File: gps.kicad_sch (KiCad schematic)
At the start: 7 parts

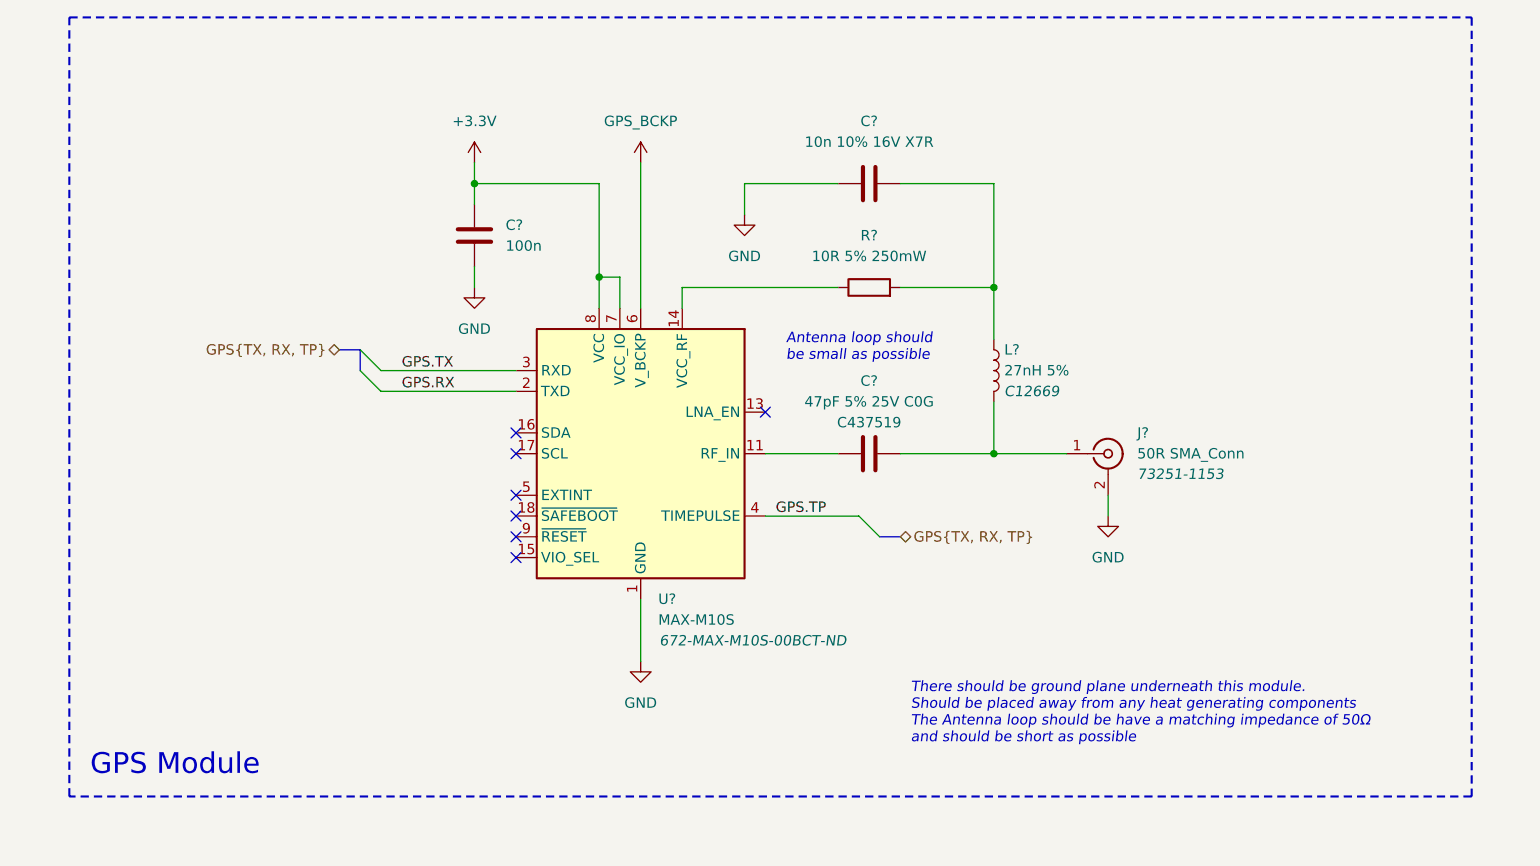
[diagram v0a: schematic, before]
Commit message: display driver update
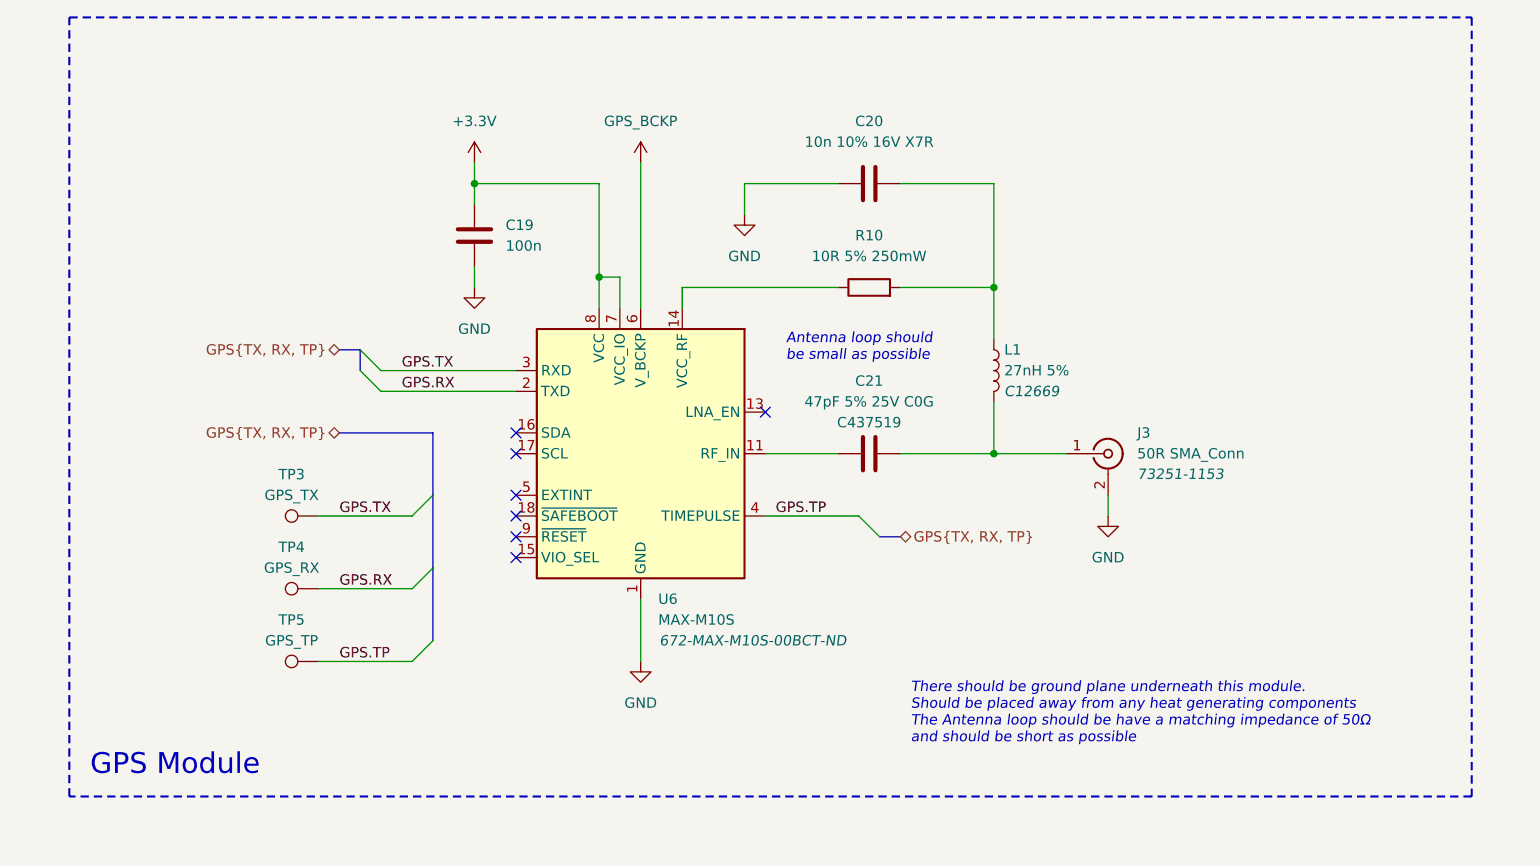
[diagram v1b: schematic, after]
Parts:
- added TP3: GPS_TX, TestPoint:TestPoint_Pad_D1.0mm, symbol Connector:TestPoint
- added TP4: GPS_RX, TestPoint:TestPoint_Pad_D1.0mm, symbol Connector:TestPoint
- added TP5: GPS_TP, TestPoint:TestPoint_Pad_D1.0mm, symbol Connector:TestPoint
- gave numbers to parts that had none: 7
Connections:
- net GPS.RX: now also TP4.1
- net GPS.TP: now also TP5.1
- net GPS.TX: now also TP3.1

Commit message: Display Driver Completion
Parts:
- C19: renamed from C21; footprint (none) -> Capacitor_SMD:C_0402_1005Metric
- renumbered C19 to C17, C20 to C18, R10 to R3, TP3 to TP1, TP4 to TP2, TP5 to TP3, U6 to U4
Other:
- moved on the sheet: TP1, TP2, TP3

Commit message: PCB Routing
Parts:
- renumbered C17 to C19, C18 to C20, C19 to C21, U4 to U5
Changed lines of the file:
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@@
 		(dnp no)
 		(fields_autoplaced yes)
-		(property "Reference" "C18"
+		(property "Reference" "C20"
 			(at 167.64 63.5 90)
 			(effects
@@
 			(project "Precision Clock"
 				(path "/c9a8ff63-a0d1-4125-9dd1-40fb53daf536/adbcdd61-c016-4293-925d-555ee31f0e50"
-					(reference "C18")
+					(reference "C20")
 					(unit 1)
 				)
@@
 		(dnp no)
 		(fields_autoplaced yes)
-		(property "Reference" "#PWR043"
+		(property "Reference" "#PWR046"
 			(at 119.38 72.39 0)
 			(effects
@@
 			(project "Precision Clock"
 				(path "/c9a8ff63-a0d1-4125-9dd1-40fb53daf536/adbcdd61-c016-4293-925d-555ee31f0e50"
-					(reference "#PWR043")
+					(reference "#PWR046")
 					(unit 1)
 				)
@@
 		(dnp no)
 		(fields_autoplaced yes)
-		(property "Reference" "#PWR048"
+		(property "Reference" "#PWR051"
 			(at 196.85 118.11 0)
 			(effects
@@
 			(project "Precision Clock"
 				(path "/c9a8ff63-a0d1-4125-9dd1-40fb53daf536/adbcdd61-c016-4293-925d-555ee31f0e50"
-					(reference "#PWR048")
+					(reference "#PWR051")
 					(unit 1)
 				)
@@
 		(on_board yes)
 		(dnp no)
-		(property "Reference" "C19"
+		(property "Reference" "C21"
 			(at 167.64 95.25 90)
 			(effects
@@
 			(project ""
 				(path "/c9a8ff63-a0d1-4125-9dd1-40fb53daf536/adbcdd61-c016-4293-925d-555ee31f0e50"
-					(reference "C19")
+					(reference "C21")
 					(unit 1)
 				)
@@
 		(dnp no)
 		(fields_autoplaced yes)
-		(property "Reference" "C17"
+		(property "Reference" "C19"
 			(at 123.19 76.1999 0)
 			(effects
@@
 			(project "Precision Clock"
 				(path "/c9a8ff63-a0d1-4125-9dd1-40fb53daf536/adbcdd61-c016-4293-925d-555ee31f0e50"
-					(reference "C17")
+					(reference "C19")
 					(unit 1)
 				)
@@
 		(dnp no)
 		(fields_autoplaced yes)
-		(property "Reference" "#PWR046"
+		(property "Reference" "#PWR049"
 			(at 139.7 135.89 0)
 			(effects
@@
 			(project "Precision Clock"
 				(path "/c9a8ff63-a0d1-4125-9dd1-40fb53daf536/adbcdd61-c016-4293-925d-555ee31f0e50"
-					(reference "#PWR046")
+					(reference "#PWR049")
 					(unit 1)
 				)
@@
 		(dnp no)
 		(fields_autoplaced yes)
-		(property "Reference" "#PWR044"
+		(property "Reference" "#PWR047"
 			(at 119.38 90.17 0)
 			(effects
@@
 			(project "Precision Clock"
 				(path "/c9a8ff63-a0d1-4125-9dd1-40fb53daf536/adbcdd61-c016-4293-925d-555ee31f0e50"
-					(reference "#PWR044")
+					(reference "#PWR047")
 					(unit 1)
 				)
@@
 		(on_board yes)
 		(dnp no)
-		(property "Reference" "#PWR045"
+		(property "Reference" "#PWR048"
 			(at 139.7 72.39 0)
 			(effects
@@
 			(project "Precision Clock"
 				(path "/c9a8ff63-a0d1-4125-9dd1-40fb53daf536/adbcdd61-c016-4293-925d-555ee31f0e50"
-					(reference "#PWR045")
+					(reference "#PWR048")
 					(unit 1)
 				)
@@
 		(on_board yes)
 		(dnp no)
-		(property "Reference" "U4"
+		(property "Reference" "U5"
 			(at 141.8433 121.92 0)
 			(effects
@@
 			(project "Precision Clock"
 				(path "/c9a8ff63-a0d1-4125-9dd1-40fb53daf536/adbcdd61-c016-4293-925d-555ee31f0e50"
-					(reference "U4")
+					(reference "U5")
 					(unit 1)
 				)
@@
 		(dnp no)
 		(fields_autoplaced yes)
-		(property "Reference" "#PWR047"
+		(property "Reference" "#PWR050"
 			(at 152.4 81.28 0)
 			(effects
@@
 			(project "Precision Clock"
 				(path "/c9a8ff63-a0d1-4125-9dd1-40fb53daf536/adbcdd61-c016-4293-925d-555ee31f0e50"
-					(reference "#PWR047")
-					(unit 1)
-				)
+					(reference "#PWR050")
+					(unit 1)
+				)

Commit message: PCB Routing
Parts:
- removed TP1: GPS_TX, TestPoint:TestPoint_Pad_D1.0mm, symbol Connector:TestPoint
- removed TP2: GPS_RX, TestPoint:TestPoint_Pad_D1.0mm, symbol Connector:TestPoint
- removed TP3: GPS_TP, TestPoint:TestPoint_Pad_D1.0mm, symbol Connector:TestPoint

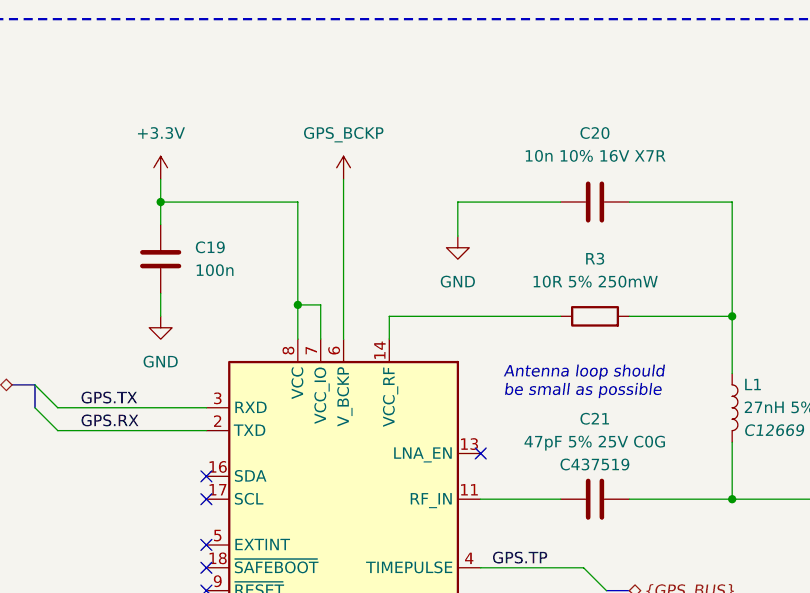
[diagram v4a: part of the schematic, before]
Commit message: Footprints added
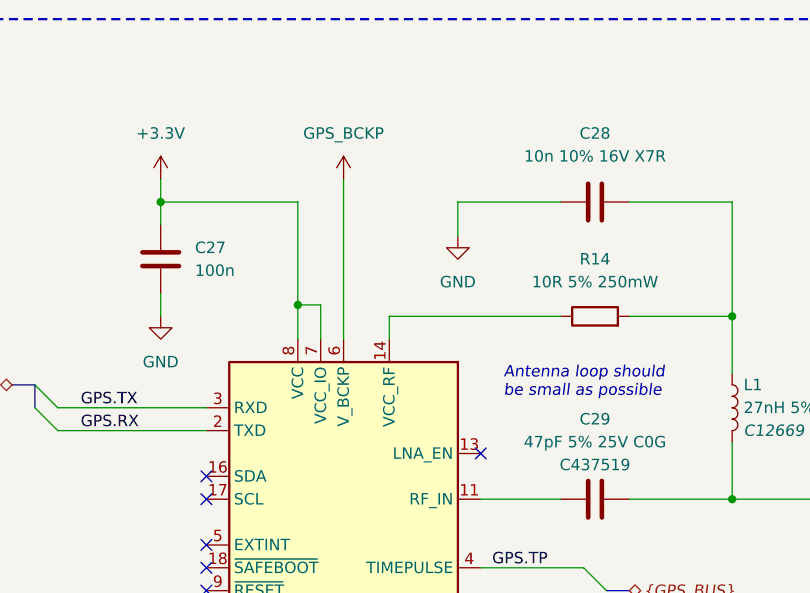
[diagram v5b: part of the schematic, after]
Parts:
- renumbered C19 to C27, C20 to C28, C21 to C29, R3 to R14
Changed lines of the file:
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@@
 		(dnp no)
 		(fields_autoplaced yes)
-		(property "Reference" "C20"
+		(property "Reference" "C28"
 			(at 167.64 63.5 90)
 			(effects
@@
 			(project "Precision Clock"
 				(path "/c9a8ff63-a0d1-4125-9dd1-40fb53daf536/adbcdd61-c016-4293-925d-555ee31f0e50"
-					(reference "C20")
+					(reference "C28")
 					(unit 1)
 				)
@@
 		(dnp no)
 		(fields_autoplaced yes)
-		(property "Reference" "#PWR046"
+		(property "Reference" "#PWR068"
 			(at 119.38 72.39 0)
 			(effects
@@
 			(project "Precision Clock"
 				(path "/c9a8ff63-a0d1-4125-9dd1-40fb53daf536/adbcdd61-c016-4293-925d-555ee31f0e50"
-					(reference "#PWR046")
+					(reference "#PWR068")
 					(unit 1)
 				)
@@
 		(dnp no)
 		(fields_autoplaced yes)
-		(property "Reference" "#PWR051"
+		(property "Reference" "#PWR073"
 			(at 196.85 118.11 0)
 			(effects
@@
 			(project "Precision Clock"
 				(path "/c9a8ff63-a0d1-4125-9dd1-40fb53daf536/adbcdd61-c016-4293-925d-555ee31f0e50"
-					(reference "#PWR051")
+					(reference "#PWR073")
 					(unit 1)
 				)
@@
 		(on_board yes)
 		(dnp no)
-		(property "Reference" "C21"
+		(property "Reference" "C29"
 			(at 167.64 95.25 90)
 			(effects
@@
 			(project ""
 				(path "/c9a8ff63-a0d1-4125-9dd1-40fb53daf536/adbcdd61-c016-4293-925d-555ee31f0e50"
-					(reference "C21")
+					(reference "C29")
 					(unit 1)
 				)
@@
 		(dnp no)
 		(fields_autoplaced yes)
-		(property "Reference" "C19"
+		(property "Reference" "C27"
 			(at 123.19 76.1999 0)
 			(effects
@@
 			(project "Precision Clock"
 				(path "/c9a8ff63-a0d1-4125-9dd1-40fb53daf536/adbcdd61-c016-4293-925d-555ee31f0e50"
-					(reference "C19")
+					(reference "C27")
 					(unit 1)
 				)
@@
 		(dnp no)
 		(fields_autoplaced yes)
-		(property "Reference" "#PWR049"
+		(property "Reference" "#PWR071"
 			(at 139.7 135.89 0)
 			(effects
@@
 			(project "Precision Clock"
 				(path "/c9a8ff63-a0d1-4125-9dd1-40fb53daf536/adbcdd61-c016-4293-925d-555ee31f0e50"
-					(reference "#PWR049")
+					(reference "#PWR071")
 					(unit 1)
 				)
@@
 		(dnp no)
 		(fields_autoplaced yes)
-		(property "Reference" "#PWR047"
+		(property "Reference" "#PWR069"
 			(at 119.38 90.17 0)
 			(effects
@@
 			(project "Precision Clock"
 				(path "/c9a8ff63-a0d1-4125-9dd1-40fb53daf536/adbcdd61-c016-4293-925d-555ee31f0e50"
-					(reference "#PWR047")
+					(reference "#PWR069")
 					(unit 1)
 				)
@@
 		(on_board yes)
 		(dnp no)
-		(property "Reference" "#PWR048"
+		(property "Reference" "#PWR070"
 			(at 139.7 72.39 0)
 			(effects
@@
 			(project "Precision Clock"
 				(path "/c9a8ff63-a0d1-4125-9dd1-40fb53daf536/adbcdd61-c016-4293-925d-555ee31f0e50"
-					(reference "#PWR048")
+					(reference "#PWR070")
 					(unit 1)
 				)
@@
 		(dnp no)
 		(fields_autoplaced yes)
-		(property "Reference" "R3"
+		(property "Reference" "R14"
 			(at 167.64 77.47 90)
 			(effects
@@
 			(project "Precision Clock"
 				(path "/c9a8ff63-a0d1-4125-9dd1-40fb53daf536/adbcdd61-c016-4293-925d-555ee31f0e50"
-					(reference "R3")
+					(reference "R14")
 					(unit 1)
 				)
@@
 		(dnp no)
 		(fields_autoplaced yes)
-		(property "Reference" "#PWR050"
+		(property "Reference" "#PWR072"
 			(at 152.4 81.28 0)
 			(effects
@@
 			(project "Precision Clock"
 				(path "/c9a8ff63-a0d1-4125-9dd1-40fb53daf536/adbcdd61-c016-4293-925d-555ee31f0e50"
-					(reference "#PWR050")
-					(unit 1)
-				)
+					(reference "#PWR072")
+					(unit 1)
+				)

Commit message: PCB Routing
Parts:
- added D12: LED, precision_clock:LED_LiteON_LTST-C281KGKT, symbol Device:LED
- added R15, R16: 510R, Resistor_SMD:R_0402_1005Metric, symbol Device:R
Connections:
- net GND: now also R15.2, R16.2
- net GPS.TP: now also D12.2 (A)
- new net: D12.1 (K), R15.1, R16.1
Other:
- note added: "3.3V OK"
- moved on the sheet: C27, C28, C29, J3, L1, R14, U5

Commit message: Major Changes
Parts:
- removed D12: LED, precision_clock:LED_LiteON_LTST-C281KGKT, symbol Device:LED
- removed R15, R16: 510R, Resistor_SMD:R_0402_1005Metric, symbol Device:R
- renumbered R14 to R16
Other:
- note removed: "3.3V OK"
- moved on the sheet: C27, C28, C29, J3, L1, R16, U5

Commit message: Verification
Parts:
- J1: renamed from J3; Digikey (none) -> 900-0732511153-ND
- renumbered C28 to C1, C27 to C11, C29 to C6, R16 to R1, U5 to U1
